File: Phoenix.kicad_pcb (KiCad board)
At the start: 2 copper layers, 86 parts, among them J1 Mini USB Female, J2 Battery Connector, J3 Pyro Connectors, Q1 2N7000, Q2 BSS84, Q3 IRFML8244TRPBF, Q4 IRFML8244TRPBF, Q5 IRFML8244TRPBF, Q6 IRFML8244TRPBF, U1 RP2040, U3 AMS1117-3.3, U4 I3G4250D, U5 MS5637-02BA03, U6 ADXL343, U8 Si4468/7, U9 L70B-M39, Y1 12MHz, Y2 30MHz

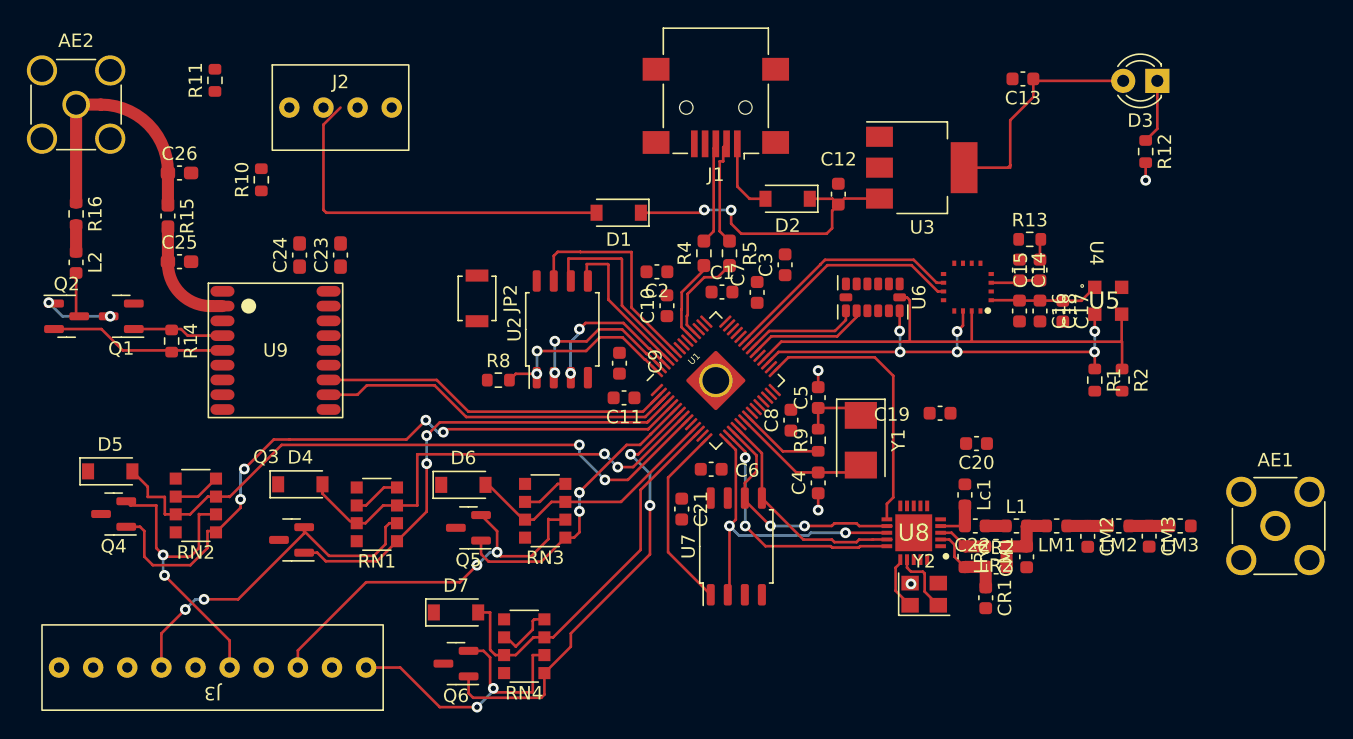
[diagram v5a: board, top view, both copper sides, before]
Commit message: Changed placements of components
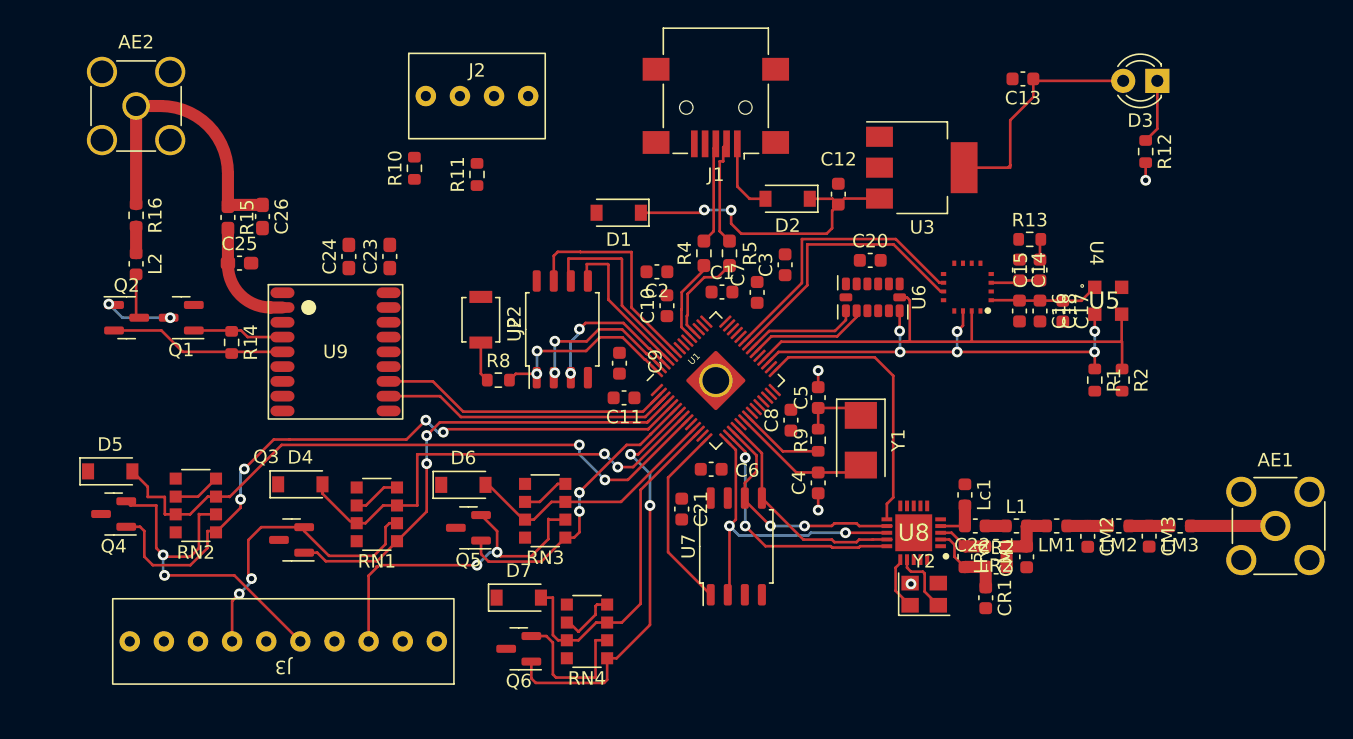
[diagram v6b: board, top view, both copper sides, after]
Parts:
- removed C19: 100nF, Capacitor_SMD:C_0603_1608Metric
- C20: value 100nF -> 470nF
- moved R11 20.7 mm to (86.4, 32.9)
- moved C20 15.8 mm to (115.6, 39.3), turned to 0 degrees
- moved R10 11.4 mm to (81.7, 32.5)
- moved J2 10.2 mm to (86.4, 27.1)
- moved C26 6.97 mm to (70.4, 36.0), turned to -90 degrees
- moved J3 5.61 mm to (71.9, 67.7)
- moved D7 4.80 mm to (89.5, 64.4)
- moved RN4 4.80 mm to (94.5, 66.9)
- moved Q6 4.80 mm to (89.5, 68.2)
- moved Q1 4.47 mm to (64.3, 43.6)
- moved L2 4.47 mm to (61.0, 39.6)
- moved R14 4.47 mm to (68.1, 45.4)
- moved R15 4.47 mm to (67.8, 36.1)
- moved R16 4.47 mm to (61.0, 36.0)
- moved AE2 4.47 mm to (61.0, 27.8)
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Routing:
- net +BATT: track 28.6 -> 0.00 mm
- net Fire 4: track 22.8 -> 11.2 mm, vias 2 -> 0
- net Net-(AE1-Pad1): track 0.00 -> 6.30 mm
- net /GPS/Rx: track 28.0 -> 22.9 mm
- net /GPS/Tx: track 27.2 -> 22.7 mm
- net Fire 3: track 29.8 -> 25.7 mm
- net Fire 1: track 26.6 -> 22.7 mm
- net Fire 2: track 23.5 -> 26.9 mm
- net /Accelerometer/Gyro1: track 18.0 -> 21.2 mm
- net /Accelerometer/Gyro2: track 17.8 -> 20.9 mm
- net Net-(JP2-Pad2): track 0.00 -> 2.99 mm
- net /GPIO & Pyro/Cont4: track 28.9 -> 26.1 mm
- net /GPIO & Pyro/Pyro4: track 33.9 -> 31.2 mm
- net Net-(AE2-Pad1): track 19.1 -> 21.7 mm

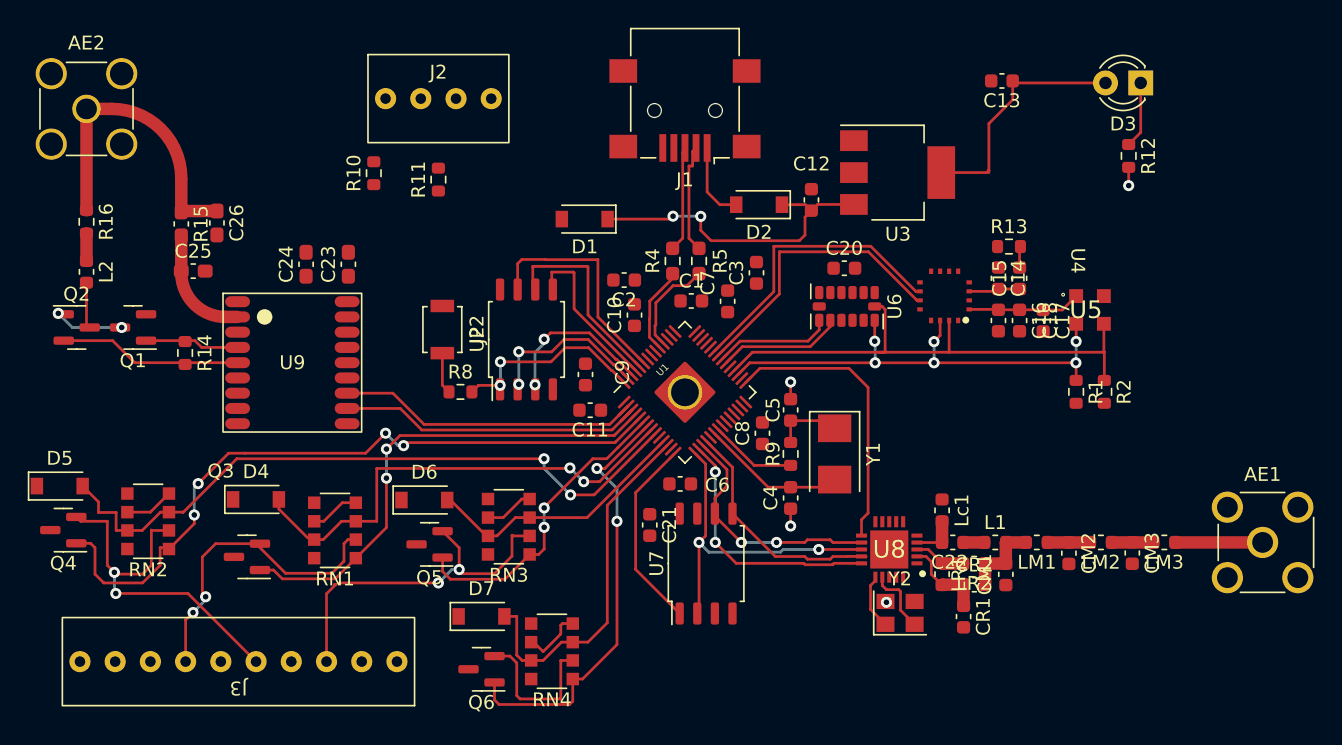
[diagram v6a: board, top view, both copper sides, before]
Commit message: Rearranged PCB to make it smaller
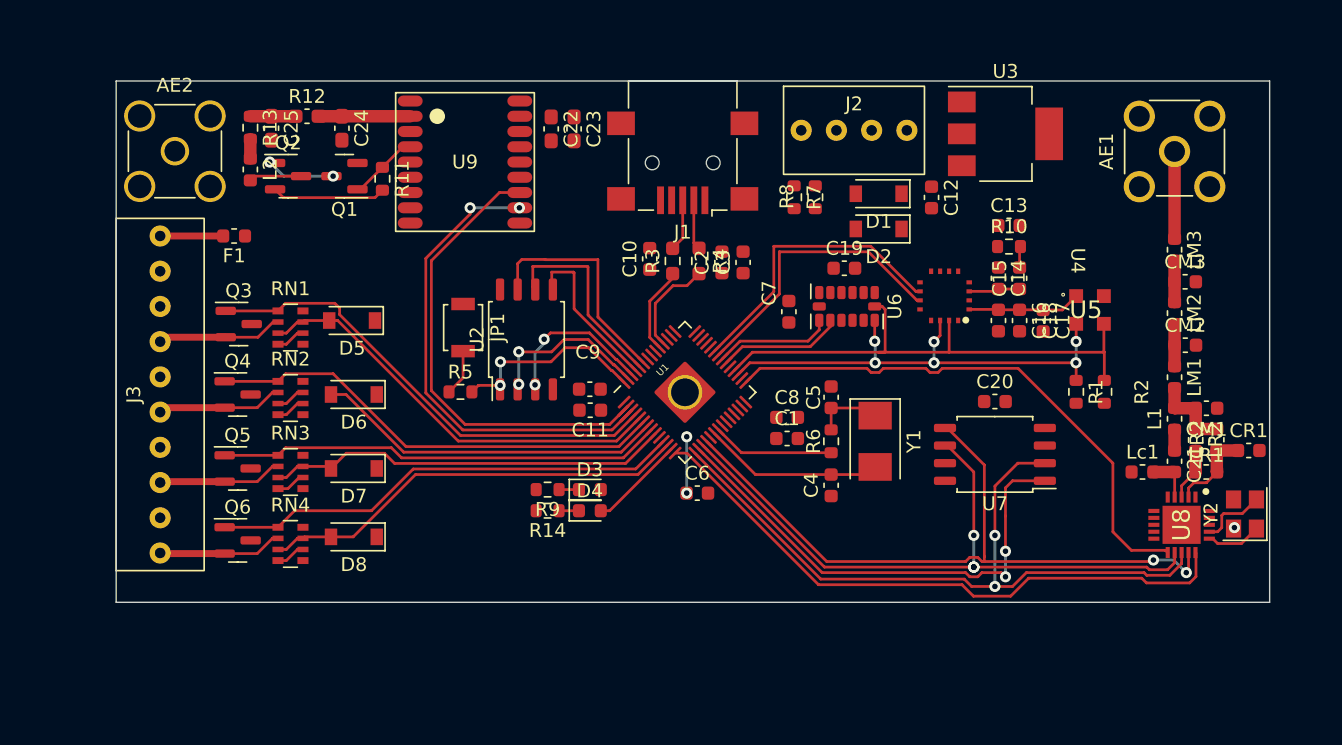
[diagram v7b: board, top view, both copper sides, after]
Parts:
- removed the C21 at (101.6, 57.8)
- removed C26: DNF, Capacitor_SMD:C_0603_1608Metric_Pad1.08x0.95mm_HandSolder
- removed the R10 at (81.7, 32.5)
- removed the R11 at (86.4, 32.9)
- removed R15: 0R, Capacitor_SMD:C_0603_1608Metric_Pad1.08x0.95mm_HandSolder
- added C20: 100n, Capacitor_SMD:C_0603_1608Metric, F.Cu at (126.5, 48.9)
- added C24: DNF, Capacitor_SMD:C_0603_1608Metric_Pad1.08x0.95mm_HandSolder, F.Cu at (79.4, 29.2)
- added D8: 1N4007, Diode_SMD:D_SOD-123, F.Cu at (80.3, 58.7)
- added F1: 2A Poly, Fuse:Fuse_0603_1608Metric, F.Cu at (71.6, 37.0)
- added R14: 470, Resistor_SMD:R_0603_1608Metric, F.Cu at (94.2, 56.8)
- added R7: 33k, Resistor_SMD:R_0603_1608Metric, F.Cu at (112.0, 34.2)
- added R8: 12k, Resistor_SMD:R_0603_1608Metric, F.Cu at (113.5, 34.2)
- added R9: 470, Resistor_SMD:R_0603_1608Metric, F.Cu at (94.2, 55.3)
- D3: footprint LED_THT:LED_D3.0mm -> LED_SMD:LED_0603_1608Metric
- D4: value 1N4007 -> GREEN; footprint Diode_SMD:D_SOD-123 -> LED_SMD:LED_0603_1608Metric
- R12: value 100 -> 0R; footprint Resistor_SMD:R_0603_1608Metric -> Capacitor_SMD:C_0603_1608Metric_Pad1.08x0.95mm_HandSolder
- RN1, RN2, RN3, RN4: footprint Resistor_SMD:R_Array_Convex_4x1206 -> Resistor_SMD:R_Array_Convex_4x0603
- moved R12 59.3 mm to (76.9, 28.4), turned to 0 degrees
- moved D3 49.4 mm to (97.3, 55.3), turned to 0 degrees
- moved J2 30.1 mm to (116.3, 29.4)
- moved AE1 28.9 mm to (139.4, 30.9), turned to 0 degrees
- moved Y2 25.9 mm to (144.5, 57.0), turned to 90 degrees
- moved D5 24.2 mm to (80.1, 43.1), turned to 180 degrees
- moved D4 24.1 mm to (97.3, 56.8)
- moved CR1 23.8 mm to (144.8, 52.5), turned to 0 degrees
- moved U7 22.3 mm to (126.5, 52.7), turned to 180 degrees
- moved C23 21.6 mm to (96.1, 29.3), turned to -90 degrees
- moved D1 21.3 mm to (118.1, 33.9)
- moved U8 21.2 mm to (140.0, 57.8), turned to -90 degrees
- moved LM3 21.1 mm to (139.4, 38.0), turned to -90 degrees
- moved LR1 20.4 mm to (141.7, 54.0), turned to 0 degrees
- moved RN4 20.4 mm to (75.7, 59.2), turned to 0 degrees
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- renumbered C20 to C19, C22 to C21, C23 to C22, C24 to C23, JP2 to JP1, R13 to R10, R14 to R11, R16 to R13, R4 to R3, R5 to R4, R8 to R5, R9 to R6
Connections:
- C25 pad 1: Net-(C25-Pad1) -> Net-(AE2-Pad1)
- D4 pad 1: +3V3 -> Net-(D4-Pad1)
- D4 pad 2: /GPIO & Pyro/Cont1 -> /GPIO & Pyro/LED
- D5 pad 2: /GPIO & Pyro/Cont2 -> /GPIO & Pyro/Cont1
- D6 pad 2: /GPIO & Pyro/Cont3 -> /GPIO & Pyro/Cont2
- D7 pad 2: /GPIO & Pyro/Cont4 -> /GPIO & Pyro/Cont3
- J3 pad 10: +BATT -> Net-(J3-Pad10)
- R12 pad 1: Net-(D3-Pad1) -> Net-(AE2-Pad1)
- R12 pad 2: GND -> Net-(C24-Pad1)
- U1 pad 11: /GPIO & Pyro/Cont3 -> /GPIO & Pyro/Pyro4
- U1 pad 13: unconnected-(U1-Pad13) -> /GPIO & Pyro/LED
- U1 pad 14: /Flash Storage/CS0 -> /Flash Storage/CS1
- U1 pad 16: /Flash Storage/CS1 -> /Flash Storage/CS0
- U1 pad 5: /GPIO & Pyro/Pyro2 -> /GPIO & Pyro/Cont1
- U1 pad 6: /GPIO & Pyro/Pyro3 -> /GPIO & Pyro/Pyro2
- U1 pad 7: /GPIO & Pyro/Pyro4 -> /GPIO & Pyro/Cont2
- U1 pad 8: /GPIO & Pyro/Cont1 -> /GPIO & Pyro/Pyro3
- U1 pad 9: /GPIO & Pyro/Cont2 -> /GPIO & Pyro/Cont3
- U9 pad 11: Net-(C25-Pad1) -> Net-(C24-Pad1)
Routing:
- net /Flash Storage/Tx: track 17.6 -> 51.4 mm, vias 0 -> 2
- net /Flash Storage/SCK: track 18.0 -> 48.4 mm, vias 2 -> 4
- net /Flash Storage/Rx: track 24.2 -> 52.3 mm
- net /Flash Storage/CS1: track 18.5 -> 44.5 mm, vias 2 -> 0
- net Net-(C12-Pad1): track 23.3 -> 0.00 mm, vias 2 -> 0
- net /GPIO & Pyro/Cont2: track 49.3 -> 27.5 mm, vias 2 -> 0
- net /Flash Storage/CS0: track 14.1 -> 35.6 mm, vias 0 -> 2
- net /Accelerometer/Radio: track 20.7 -> 39.8 mm
- net Net-(AE2-Pad1): track 21.7 -> 3.23 mm
- net Fire 2: track 26.9 -> 9.08 mm, vias 2 -> 0
- net /GPIO & Pyro/Pyro2: track 51.0 -> 33.4 mm, vias 4 -> 0
- net Fire 3: track 25.7 -> 8.98 mm, vias 2 -> 0
- net Fire 1: track 22.7 -> 9.08 mm, vias 2 -> 0
- net +3V3: track 17.6 -> 4.08 mm, vias 0 -> 2
- net /GPS/Rx: track 22.9 -> 35.9 mm, vias 0 -> 2
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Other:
- board outline added: 83.2 x 37.6 mm
- board text added: "I wont bother connecting the antenna until we actually know what it is - Will"
